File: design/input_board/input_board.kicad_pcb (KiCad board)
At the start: 6 copper layers, 65.2 x 117.2 mm, 178 parts, among them IC1 LM5157RTER, IC10 ADS8860IDGSR, IC2 TMUX7349FPWR, IC3 TMUX7349FPWR, IC4 TMUX7349FPWR, IC5 TMUX7349FPWR, IC6 MUX509IPW, IC7 MUX509IPW, IC8 MUX36D08IPW, IC9 MUX508IPW, J1 Screw_Terminal_01x02, J10 Programmer, J11 Screw_Terminal_01x02, J2 Screw_Terminal_01x03, J3 Screw_Terminal_01x08, J4 Screw_Terminal_01x08, J5 Screw_Terminal_01x08, J6 Screw_Terminal_01x08, J7 Screw_Terminal_01x02, J8 USB_B, J9 CAN, Q1 CSD19537Q3, Q2 BSS138, U1 TPS26631PWP, U10 INA849DGK, U11 INA849DGK, U12 REF6050xDGK, U13 uA7805, U14 TPS76933, U15 MCP2562, U16 STM32H750ZBTx, U17 TPS565201, U18 INA180A3, U2 TPS7A4701xRGW, U3 INA290A3, U4 INA849DGK, U5 INA849DGK, U6 INA849DGK, U7 INA849DGK, U8 INA849DGK, U9 INA849DGK

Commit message: More footprints
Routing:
- net +2V: track 138.1 -> 288.6 mm, vias 26 -> 28
- net Net-(U18-IN+): track 43.8 -> 50.9 mm
- net VDDA: track 100.7 -> 105.5 mm
- net GND: track 119.5 -> 116.8 mm
- net /Frontend/IN8-: track 13.3 -> 15.9 mm
- net /Frontend/INPUT_A0: track 135.1 -> 137.0 mm
- net /Frontend/IN14+: track 12.1 -> 13.8 mm
- net /Frontend/IN10+: track 12.1 -> 13.8 mm
- net /Frontend/FAULT_1..4: track 61.2 -> 62.9 mm
- net /Frontend/IN9+: track 17.4 -> 19.0 mm
- net Net-(IC1-VCC): track 3.73 -> 5.33 mm
- net /12V Input/IN_SYS: track 13.7 -> 15.2 mm
- net +5V: track 215.3 -> 216.8 mm
- net +12V: track 47.8 -> 49.3 mm
- net Net-(U3-VO): track 2.27 -> 3.41 mm
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
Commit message: Layout v2; better
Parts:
- removed C2, C3: 10uF, Capacitor_SMD:C_0805_2012Metric_Pad1.18x1.45mm_HandSolder
- added C70: 0.1uF, Capacitor_SMD:C_0805_2012Metric_Pad1.18x1.45mm_HandSolder, B.Cu at (63.4, 70.9)
- added C71: 0.1uF, Capacitor_SMD:C_0805_2012Metric_Pad1.18x1.45mm_HandSolder, F.Cu at (92.3, 79.1)
- added G***: LOGO, input_board:Logo_SilkScreen_15mm, F.Cu at (97.1, 84.7)
- C10, C11, C12, C4, C5, C56, C57, C6, C68, C7, C8, D6, IC1, L1, Q1, Q2, R10, R11, R12, R16, R17, R20, R22, R23, R24, R25, R26, R27, R28, R29, R30, R5, R6, R7, R9, U1, U16, U2: moved to F.Cu
- C18, C19, C20, C21, C23, C24, C25, C34, C37, C38, C39, C41, C42, C43, C44, C46, C48, C50, C53, C65, C66, C67, C69, IC10, IC2, IC3, IC4, IC5, IC6, IC7, IC8, IC9, J10, JP1, R1, R2, R3, R32, R33, R34, R35, R36, R37, R38, R39, R4, R40, R44, R45, R46, RN1, RN2, U10, U11, U12, U14, U18, U4, U5, U6, U7, U8, U9: moved to B.Cu
- J2: footprint TerminalBlock_Phoenix:TerminalBlock_Phoenix_MKDS-1,5-3-5.08_1x03_P5.08mm_Horizontal -> Connector_PinHeader_2.54mm:PinHeader_1x03_P2.54mm_Vertical
- J9: footprint TerminalBlock_Phoenix:TerminalBlock_Phoenix_MPT-0,5-3-2.54_1x03_P2.54mm_Horizontal -> Connector_PinHeader_2.54mm:PinHeader_1x03_P2.54mm_Vertical
- moved H2 121.2 mm to (50.8, 101.6)
- moved C17 110.5 mm to (51.1, 65.8), turned to -90 degrees
- moved C16 108.2 mm to (51.1, 61.7)
- moved J5 107.0 mm to (57.1, 57.1), turned to 0 degrees
- moved TP5 106.2 mm to (52.6, 56.9)
- moved H1 104.1 mm to (50.8, 50.8)
- moved IC3 104.1 mm to (56.2, 63.4), turned to 180 degrees
- moved C22 86.4 mm to (73.4, 62.0), turned to 90 degrees
- moved J6 86.3 mm to (79.0, 57.1), turned to 0 degrees
- moved C29 84.5 mm to (72.6, 75.7), turned to 0 degrees
- moved C24 83.6 mm to (50.8, 81.0), turned to 180 degrees
- moved J3 82.5 mm to (57.1, 95.2), turned to 0 degrees
- moved C23 82.2 mm to (73.4, 66.0), turned to -90 degrees
- moved IC2 81.4 mm to (56.8, 89.3), turned to 0 degrees
- moved F1 80.7 mm to (153.9, 56.4), turned to -90 degrees
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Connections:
- F1 pad 1: Net-(J1-Pin_2) -> Net-(J1-Pin_1)
- J1 pad 1: GND -> Net-(J1-Pin_1)
- J1 pad 2: Net-(J1-Pin_2) -> GND
- U16 pad 1: /Frontend/FAULT_9..12 -> unconnected-(U16-PE2-Pad1)
- U16 pad 10: /Frontend/EN_1..4 -> unconnected-(U16-PF0-Pad10)
- U16 pad 11: /Frontend/INPUT_A0 -> unconnected-(U16-PF1-Pad11)
- U16 pad 12: /Frontend/INPUT_A1 -> unconnected-(U16-PF2-Pad12)
- U16 pad 13: /Frontend/SEL_IN_2 -> unconnected-(U16-PF3-Pad13)
- U16 pad 14: /Frontend/SEL_IN_3 -> unconnected-(U16-PF4-Pad14)
- U16 pad 141: /Frontend/FAULT_1..4 -> unconnected-(U16-PE0-Pad141)
- U16 pad 142: /Frontend/FAULT_5..8 -> unconnected-(U16-PE1-Pad142)
- U16 pad 15: /Frontend/SINGLE_DIFF_0 -> unconnected-(U16-PF5-Pad15)
- U16 pad 18: /Frontend/SINGLE_DIFF_1 -> unconnected-(U16-PF6-Pad18)
- U16 pad 19: /Amplifiers/AMP_SEL_0 -> unconnected-(U16-PF7-Pad19)
- U16 pad 2: /Frontend/FAULT_13..16 -> unconnected-(U16-PE3-Pad2)
- U16 pad 20: /Amplifiers/AMP_SEL_1 -> unconnected-(U16-PF8-Pad20)
- U16 pad 21: /Amplifiers/AMP_SEL_2 -> /Frontend/INPUT_A1
- U16 pad 22: unconnected-(U16-PF10-Pad22) -> /Frontend/INPUT_A0
- U16 pad 23: unconnected-(U16-PH0-Pad23) -> /12V Input/~{FLT_12V}
- U16 pad 24: unconnected-(U16-PH1-Pad24) -> /Frontend/SF_9..12
- U16 pad 28: unconnected-(U16-PC2_C-Pad28) -> /Frontend/FAULT_13..16
- U16 pad 3: /Frontend/SF_1..4 -> unconnected-(U16-PE4-Pad3)
- U16 pad 34: unconnected-(U16-PA0-Pad34) -> /Frontend/SF_13..16
- U16 pad 35: /12V Input/~{FLT_12V} -> /Frontend/FAULT_9..12
- U16 pad 4: /Frontend/SF_5..8 -> unconnected-(U16-PE5-Pad4)
- U16 pad 44: unconnected-(U16-PC4-Pad44) -> /Frontend/EN_1..4
- U16 pad 45: unconnected-(U16-PC5-Pad45) -> /Amplifiers/AMP_SEL_0
- U16 pad 46: unconnected-(U16-PB0-Pad46) -> /Amplifiers/AMP_SEL_2
- U16 pad 47: unconnected-(U16-PB1-Pad47) -> /Amplifiers/AMP_SEL_1
- U16 pad 5: /Frontend/SF_9..12 -> unconnected-(U16-PE6-Pad5)
- U16 pad 7: /Frontend/SF_13..16 -> unconnected-(U16-PC13-Pad7)
- U16 pad 74: unconnected-(U16-PB13-Pad74) -> /Frontend/FAULT_5..8
- U16 pad 75: unconnected-(U16-PB14-Pad75) -> /Frontend/SF_5..8
- U16 pad 76: unconnected-(U16-PB15-Pad76) -> /Frontend/FAULT_1..4
- U16 pad 77: unconnected-(U16-PD8-Pad77) -> /Frontend/SF_1..4
- U16 pad 78: unconnected-(U16-PD9-Pad78) -> /Frontend/SEL_IN_2
- U16 pad 79: unconnected-(U16-PD10-Pad79) -> /Frontend/SEL_IN_3
- U16 pad 80: unconnected-(U16-PD11-Pad80) -> /Frontend/SINGLE_DIFF_1
- U16 pad 81: unconnected-(U16-PD12-Pad81) -> /Frontend/SINGLE_DIFF_0
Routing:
- net +2V: track 288.6 -> 59.4 mm, vias 28 -> 45
- net +5V: track 216.8 -> 75.3 mm, vias 2 -> 5
- net /Frontend/SINGLE_DIFF_0: track 35.2 -> 116.7 mm, vias 1 -> 3
- net +12V: track 49.3 -> 130.7 mm, vias 61 -> 20
- net /Frontend/SINGLE_DIFF_1: track 32.7 -> 111.1 mm, vias 1 -> 3
- net /Frontend/SEL_IN_2: track 51.0 -> 105.8 mm, vias 1 -> 2
- net VDDA: track 105.5 -> 51.8 mm, vias 24 -> 32
- net /Frontend/SEL_IN_3: track 47.4 -> 100.9 mm, vias 1 -> 2
- net Net-(U18-IN+): track 50.9 -> 0.97 mm, vias 0 -> 1
- net /Frontend/INPUT_A1: track 128.0 -> 174.9 mm, vias 4 -> 6
- net /Frontend/FAULT_1..4: track 62.9 -> 101.7 mm, vias 1 -> 3
- net /Frontend/IN_9..12+: track 49.4 -> 11.3 mm, vias 4 -> 0
- net /Frontend/IN5-: track 38.3 -> 6.33 mm
- net /Frontend/IN1-: track 38.4 -> 6.60 mm
- net /12V Input/IN_SYS: track 15.2 -> 46.4 mm, vias 0 -> 6
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- added copper zone on F.Cu, net +2V
- added copper zone on In2.Cu, net +2V
- added copper zone on F.Cu, net /12V Input/IN_SYS
- added copper zone on In3.Cu, net GND
- added copper zone on F.Cu, net Net-(D6-A)
- added copper zone on F.Cu, net Net-(U18-IN+)
- added copper zone on B.Cu, net Net-(U3-IN+)
- added copper zone on F.Cu, net Net-(U3-IN+)
- added copper zone on In2.Cu, net VDDA
- added copper zone on F.Cu, net V_BOOST
- removed copper zone on B.Cu, net +12V
- removed copper zone on In3.Cu, net +12V
- removed copper zone on In3.Cu, net +2V
- removed copper zone on B.Cu, net /12V Input/IN_SYS
- removed copper zone on B.Cu, net Net-(D6-A)
- removed copper zone on B.Cu, net Net-(Q1-D)
- removed copper zone on In3.Cu, net VDDA
- removed copper zone on B.Cu, net V_BOOST
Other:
- board size 65.2 x 117.2 mm -> 111.8 x 61 mm
- board text added: "+12V"
- board text added: "+2V"
- board text added: "+VDDA"
- board text added: "AGND"
- board text added: "Achilles"
- board text added: "BOOST"
- board text added: "CANH"
- board text added: "CANL"
- board text added: "GND"
- board text added: "IN1+"
- board text added: "IN1-"
- board text added: "Joe Dolina 2025-07"

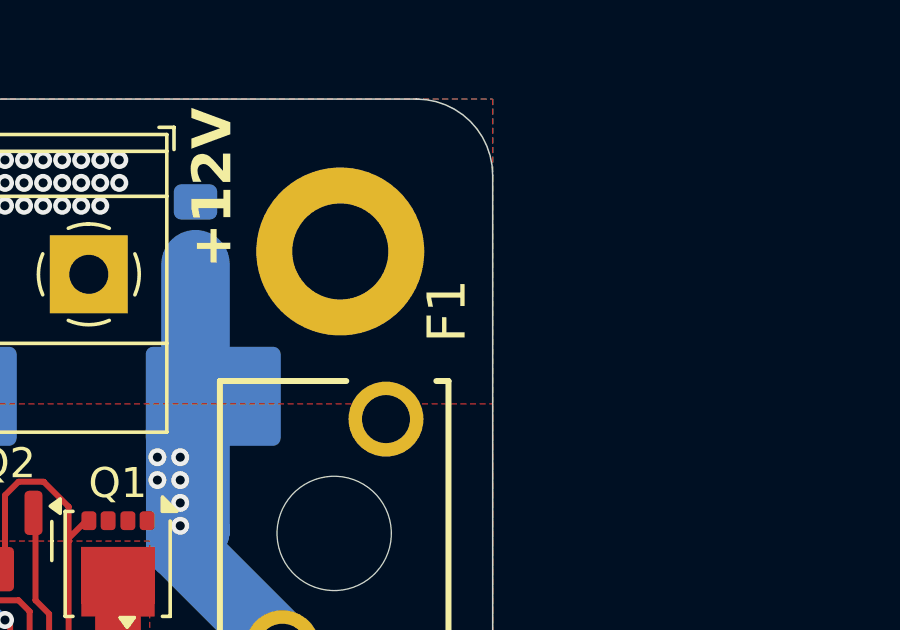
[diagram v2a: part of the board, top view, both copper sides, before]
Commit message: Add values for charge bucket filter
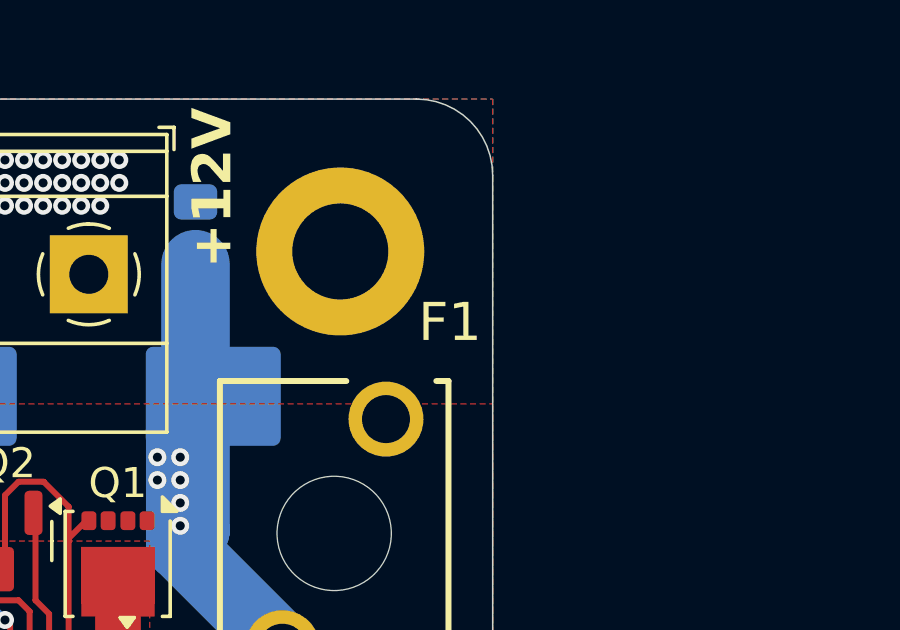
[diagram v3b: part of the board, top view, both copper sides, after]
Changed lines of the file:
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@@
 		(tags "Fuse")
 		(property "Reference" "F1"
-			(at -3.6068 -2.032 90)
+			(at -3.2258 -2.1336 180)
 			(layer "F.SilkS")
 			(effects
